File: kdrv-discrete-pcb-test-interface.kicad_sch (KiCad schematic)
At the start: 0 parts

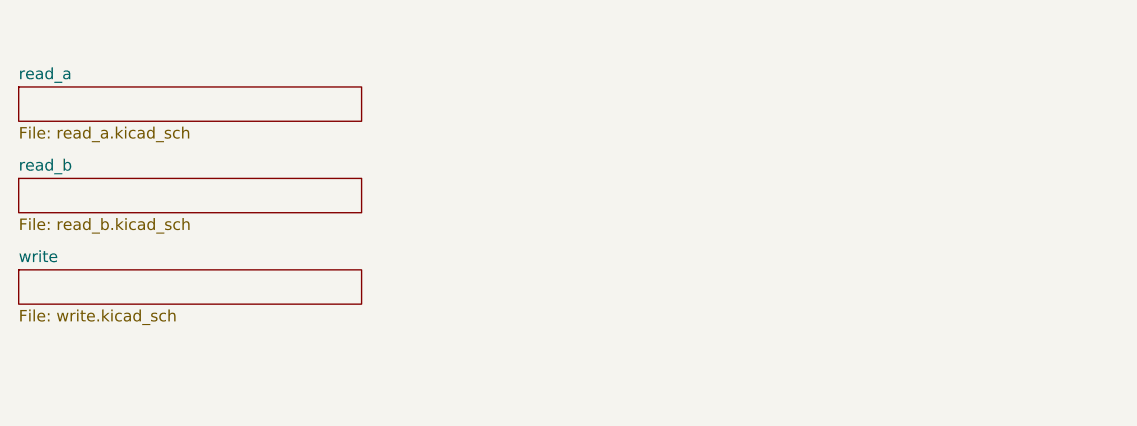
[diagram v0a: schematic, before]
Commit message: Schematic mostly finished.  Still need to make the PCIe connector layouts.
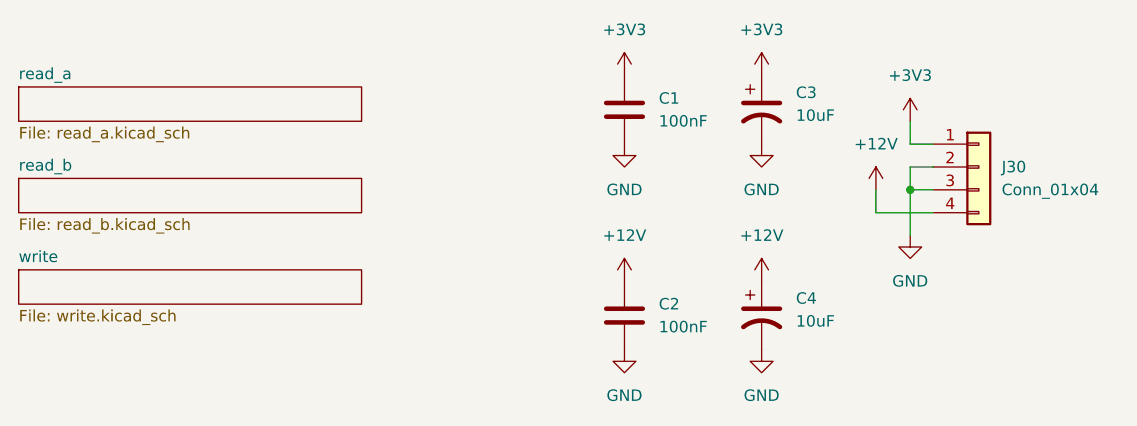
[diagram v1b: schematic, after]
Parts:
- added C1, C2: 100nF, symbol Device:C
- added C3, C4: 10uF, symbol Device:C_Polarized_US
- added J30: Conn_01x04, symbol Connector_Generic:Conn_01x04
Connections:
- new net +12V: C2.1, C4.1, J30.4 (Pin_4)
- new net +3V3: C1.1, C3.1, J30.1 (Pin_1)
- new net GND: C1.2, C2.2, C3.2, C4.2, J30.2 (Pin_2), J30.3 (Pin_3)
